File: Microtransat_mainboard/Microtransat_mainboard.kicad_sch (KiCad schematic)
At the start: 16 parts, among them J10 Conn_01x04, J2 Conn_01x02, J4 Conn_01x04, J5 Conn_01x05, J7 Conn_01x05, J9 Conn_01x04, SW1 SW_SPST, U5 SD Card Module

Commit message: add estop stuff kinda
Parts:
- removed J7: Conn_01x05, symbol Connector_Generic:Conn_01x05
- added J1: Conn_01x08, symbol Connector_Generic:Conn_01x08
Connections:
- net +5V: now also J1.1 (Pin_1)
- net GND: now also J1.2 (Pin_2)
- net INPWM0: now also J1.3 (Pin_3)
- net INPWM1: now also J1.4 (Pin_4)
- net MODE: now also J1.5 (Pin_5)
- net GPIO20: now reaches A1.26 (GPIO20)
- net GPIO21: now reaches A1.27 (GPIO21)
- new net eSTOPIN: J1.6 (Pin_6)
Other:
- sheet LED Interface renamed Relay Board Interface
- added sheet eStop Reading (estop_reading.kicad_sch)
- added sheet eStop Trigger (estop_trigger.kicad_sch)
- note removed: "Add all of the pins (6 total)"
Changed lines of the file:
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@@
 		)
 	)
-	(text "Add all of the pins (6 total)"
-		(exclude_from_sim no)
-		(at 82.55 128.016 0)
-		(effects
-			(font
-				(size 1.27 1.27)
-			)
-		)
-	)
 	(text "uses spi\nCS0\n"
 		(exclude_from_sim no)
@@
 		)
 	)
+	(label "GPIO20"
+		(at 144.78 45.72 0)
+		(effects
+			(font
+				(size 1.27 1.27)
+			)
+			(justify left bottom)
+		)
+	)
 	(label "PPS"
 		(at 172.72 114.3 180)
@@
 		)
 	)
+	(label "GPIO21"
+		(at 151.13 60.96 0)
+		(effects
+			(font
+				(size 1.27 1.27)
+			)
+			(justify left bottom)
+		)
+	)
 	(label "SCL"
 		(at 111.76 147.32 180)
@@
 		)
 	)
+	(label "GPIO20"
+		(at 218.44 119.38 0)
+		(effects
+			(font
+				(size 1.27 1.27)
+			)
+			(justify left bottom)
+		)
+	)
 	(label "CS1"
 		(at 51.435 186.69 0)
@@
 		)
 	)
+	(label "eSTOPIN"
+		(at 72.39 139.7 180)
+		(effects
+			(font
+				(size 1.27 1.27)
+			)
+			(justify right bottom)
+		)
+	)
 	(label "VREF"
 		(at 218.44 134.62 0)
@@
 		)
 	)
+	(label "GPIO21"
+		(at 218.44 121.92 0)
+		(effects
+			(font
+				(size 1.27 1.27)
+			)
+			(justify left bottom)
+		)
+	)
 	(label "MODE"
 		(at 172.72 127 180)
@@
 		)
 	)
+	(label "eSTOPIN"
+		(at 118.11 45.72 180)
+		(effects
+			(font
+				(size 1.27 1.27)
+			)
+			(justify right bottom)
+		)
+	)
 	(label "SDA"
 		(at 172.72 121.92 180)
@@
 	)
 	(symbol
-		(lib_id "Connector_Generic:Conn_01x05")
-		(at 77.47 132.08 0)
-		(unit 1)
-		(exclude_from_sim no)
-		(in_bom yes)
-		(on_board yes)
-		(dnp no)
-		(fields_autoplaced yes)
-		(property "Reference" "J7"
-			(at 80.01 130.8099 0)
-			(effects
-				(font
-					(size 1.27 1.27)
-				)
-				(justify left)
-			)
-		)
-		(property "Value" "Conn_01x05"
-			(at 80.01 133.3499 0)
-			(effects
-				(font
-					(size 1.27 1.27)
-				)
-				(justify left)
-			)
-		)
-		(property "Footprint" ""
-			(at 77.47 132.08 0)
-			(effects
-				(font
-					(size 1.27 1.27)
-				)
-				(hide yes)
-			)
-		)
-		(property "Datasheet" "~"
-			(at 77.47 132.08 0)
-			(effects
-				(font
-					(size 1.27 1.27)
-				)
-				(hide yes)
-			)
-		)
-		(property "Description" "Generic connector, single row, 01x05, script generated (kicad-library-utils/schlib/autogen/connector/)"
-			(at 77.47 132.08 0)
-			(effects
-				(font
-					(size 1.27 1.27)
-				)
-				(hide yes)
-			)
-		)
-		(pin "2"
-		)
-		(pin "1"
-		)
-		(pin "5"
-		)
-		(pin "3"
-		)
-		(pin "4"
-		)
-		(instances
-			(project ""
-				(path "/89914625-be83-416e-bb0d-b792f59b4aa6"
-					(reference "J7")
-					(unit 1)
-				)
-			)
-		)
-	)
-	(symbol
 		(lib_id "power:+5V")
 		(at 190.5 83.82 0)
@@
 	)
 	(symbol
+		(lib_id "Connector_Generic:Conn_01x08")
+		(at 77.47 134.62 0)
+		(unit 1)
+		(exclude_from_sim no)
+		(in_bom yes)
+		(on_board yes)
+		(dnp no)
+		(fields_autoplaced yes)
+		(property "Reference" "J1"
+			(at 80.01 134.6199 0)
+			(effects
+				(font
+					(size 1.27 1.27)
+				)
+				(justify left)
+			)
+		)
+		(property "Value" "Conn_01x08"
+			(at 80.01 137.1599 0)
+			(effects
+				(font
+					(size 1.27 1.27)
+				)
+				(justify left)
+			)
+		)
+		(property "Footprint" ""
+			(at 77.47 134.62 0)
+			(effects
+				(font
+					(size 1.27 1.27)
+				)
+				(hide yes)
+			)
+		)
+		(property "Datasheet" "~"
+			(at 77.47 134.62 0)
+			(effects
+				(font
+					(size 1.27 1.27)
+				)
+				(hide yes)
+			)
+		)
+		(property "Description" "Generic connector, single row, 01x08, script generated (kicad-library-utils/schlib/autogen/connector/)"
+			(at 77.47 134.62 0)
+			(effects
+				(font
+					(size 1.27 1.27)
+				)
+				(hide yes)
+			)
+		)
+		(pin "5"
+		)
+		(pin "1"
+		)
+		(pin "2"
+		)
+		(pin "3"
+		)
+		(pin "4"
+		)
+		(pin "6"
+		)
+		(pin "7"
+		)
+		(pin "8"
+		)
+		(instances
+			(project ""
+				(path "/89914625-be83-416e-bb0d-b792f59b4aa6"
+					(reference "J1")
+					(unit 1)
+				)
+			)
+		)
+	)
+	(symbol
 		(lib_id "Device:R")
 		(at 24.13 82.55 0)
@@
 			(color 0 0 0 0.0000)
 		)
-		(property "Sheetname" "LED Interface"
+		(property "Sheetname" "Relay Board Interface"
 			(at 241.3 107.2384 0)
 			(effects
@@
 	)
 	(sheet
+		(at 118.11 58.42)
+		(size 33.02 5.08)
+		(exclude_from_sim no)
+		(in_bom yes)
+		(on_board yes)
+		(dnp no)
+		(fields_autoplaced yes)
+		(stroke
+			(width 0.1524)
+			(type solid)
+		)
+		(fill
+			(color 0 0 0 0.0000)
+		)
+		(property "Sheetname" "eStop Reading"
+			(at 118.11 57.7084 0)
+			(effects
+				(font
+					(size 1.27 1.27)
+				)
+				(justify left bottom)
+			)
+		)
+		(property "Sheetfile" "estop_reading.kicad_sch"
+			(at 118.11 64.0846 0)
+			(effects
+				(font
+					(size 1.27 1.27)
+				)
+				(justify left top)
+			)
+		)
+		(pin "estop_signal" output
+			(at 151.13 60.96 0)
+			(effects
+				(font
+					(size 1.27 1.27)
+				)
+				(justify right)
+			)
+		)
+		(instances
+			(project "Microtransat_mainboard"
+				(path "/89914625-be83-416e-bb0d-b792f59b4aa6"
+					(page "4")
+				)
+			)
+		)
+	)
+	(sheet
 		(at 121.92 105.41)
 		(size 25.4 10.16)
@@
 				)
 			)
+		)
+	)
+	(sheet
+		(at 118.11 43.18)
+		(size 26.67 5.08)
+		(exclude_from_sim no)
+		(in_bom yes)
+		(on_board yes)
+		(dnp no)
+		(fields_autoplaced yes)
+		(stroke
+			(width 0.1524)
+			(type solid)
+		)
+		(fill
+			(color 0 0 0 0.0000)
+		)
+		(property "Sheetname" "eStop Trigger"
+			(at 118.11 42.4684 0)
+			(effects
+				(font
+					(size 1.27 1.27)
+				)
+				(justify left bottom)
+			)
+		)
+		(property "Sheetfile" "estop_trigger.kicad_sch"
+			(at 118.11 48.8446 0)
+			(effects
+				(font
+					(size 1.27 1.27)
+				)
+				(justify left top)
+			)
+		)
+		(pin "OUT" output
+			(at 144.78 45.72 0)
+			(effects
+				(font
+					(size 1.27 1.27)
+				)
+				(justify right)
+			)
+		)
+		(pin "RC_IN" input
+			(at 118.11 45.72 180)
+			(effects
+				(font
+					(size 1.27 1.27)
+				)
+				(justify left)
+			)
+		)
+		(instances
+			(project "Microtransat_mainboard"
+				(path "/89914625-be83-416e-bb0d-b792f59b4aa6"
+					(page "5")
+				)
+			)

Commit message: puh
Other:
- sheet Relay Board Interface ports: added eStopTrigger; removed none
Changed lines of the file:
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@@
 	(wire
 		(pts
+			(xy 262.89 110.49) (xy 266.7 110.49)
+		)
+		(stroke
+			(width 0)
+			(type default)
+		)
+	)
+	(wire
+		(pts
 			(xy 24.13 86.36) (xy 24.13 87.63)
 		)
@@
 	(wire
 		(pts
+			(xy 266.7 45.72) (xy 144.78 45.72)
+		)
+		(stroke
+			(width 0)
+			(type default)
+		)
+	)
+	(wire
+		(pts
+			(xy 266.7 110.49) (xy 266.7 45.72)
+		)
+		(stroke
+			(width 0)
+			(type default)
+		)
+	)
+	(wire
+		(pts
 			(xy 24.13 97.79) (xy 24.13 100.33)
 		)
@@
 			)
 		)
+		(pin "eStopTrigger" input
+			(at 262.89 110.49 0)
+			(effects
+				(font
+					(size 1.27 1.27)
+				)
+				(justify right)
+			)
+		)

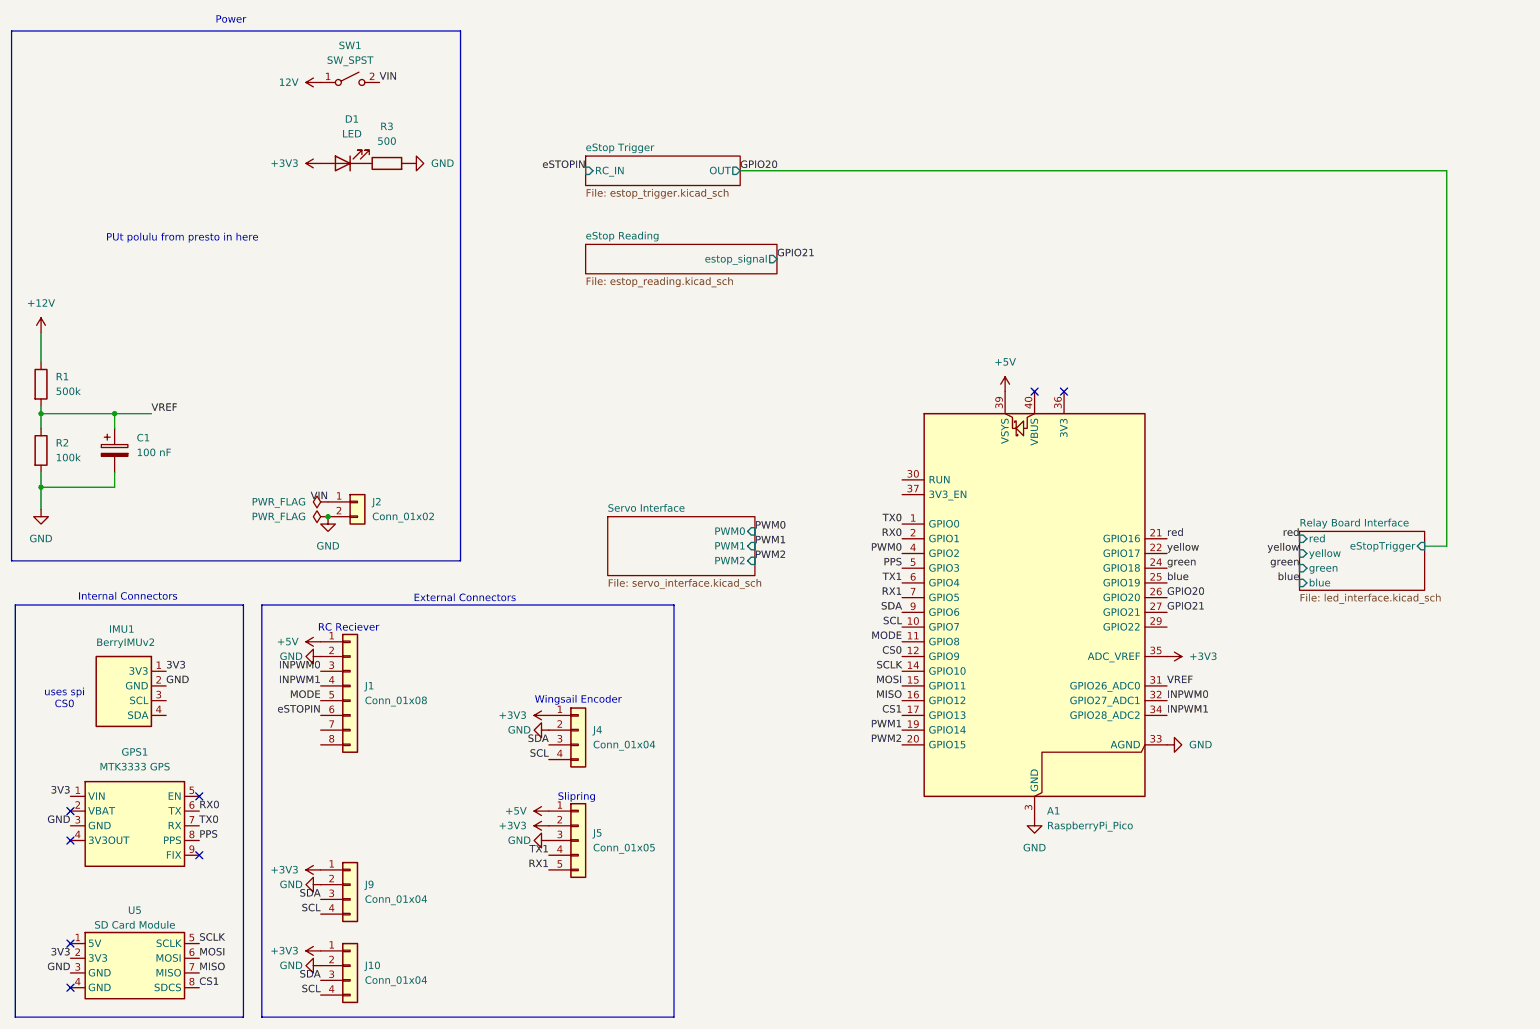
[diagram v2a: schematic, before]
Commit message: Added new IMU to the schematic + new PWM
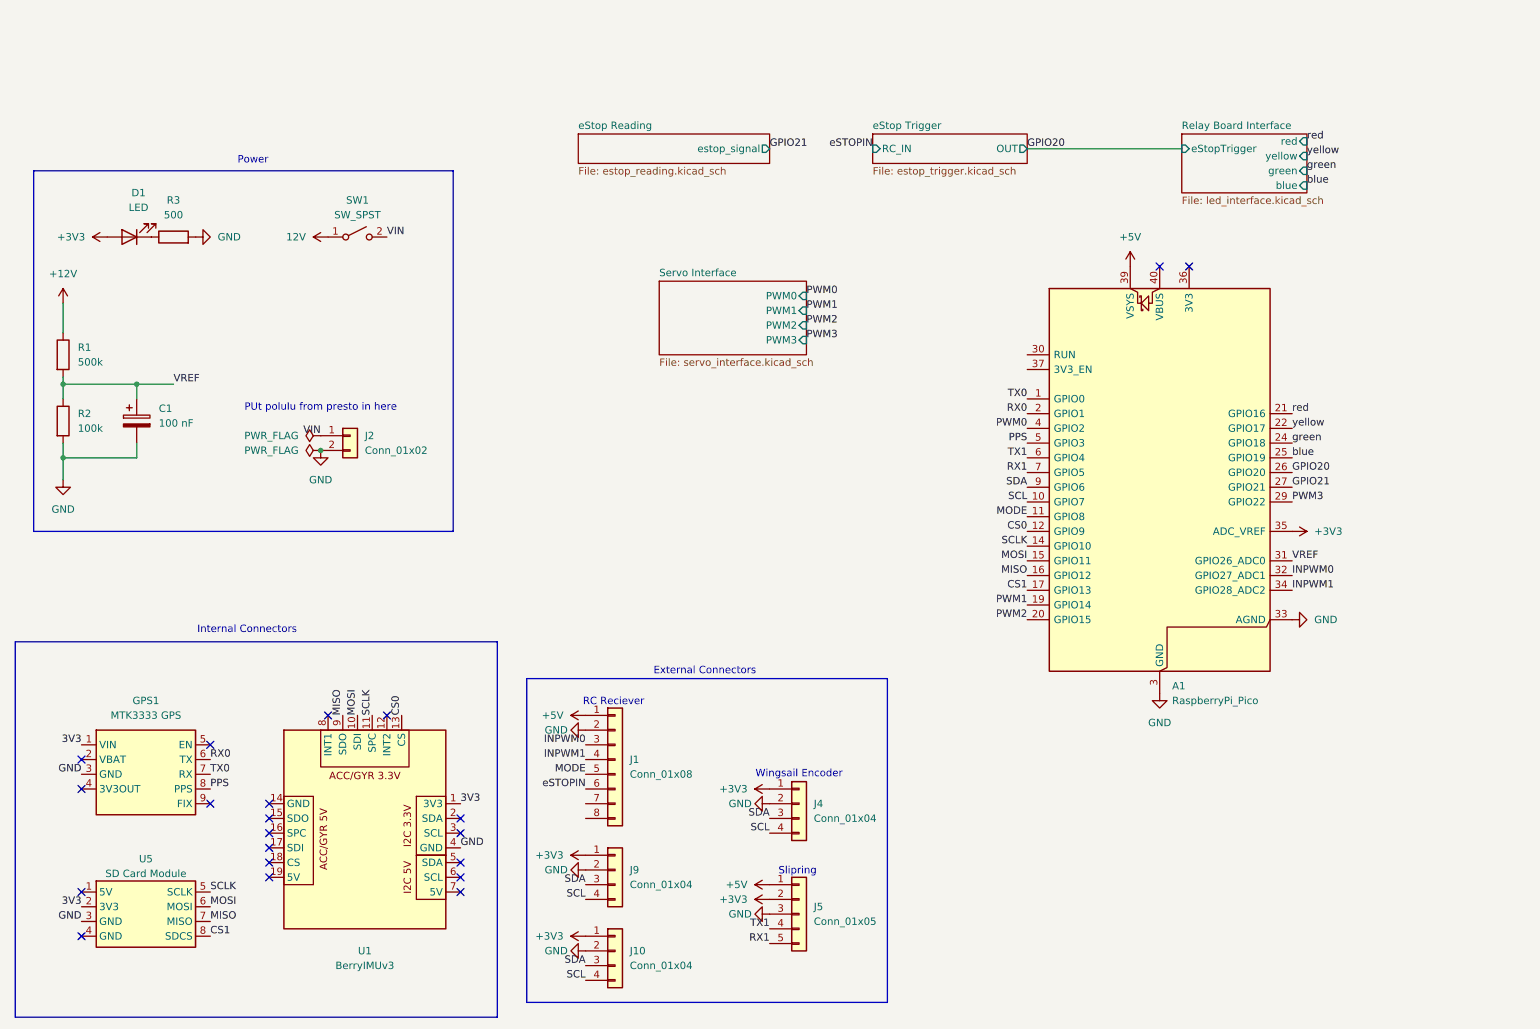
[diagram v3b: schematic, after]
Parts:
- removed IMU1: BerryIMUv2, symbol Microtransat:BerryIMUv2
- added U1: BerryIMUv3, Microtransat:BerryIMUv3, symbol Microtransat:BerryIMUv3
- GPS1: footprint (none) -> Microtransat:MTK3333
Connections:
- net 3V3: now also U1.1 (3V3)
- net CS0: now also U1.13 (CS)
- net GND: now also U1.4 (GND)
- net MISO: now also U1.9 (SDO)
- net MOSI: now also U1.10 (SDI)
- net SCLK: now also U1.11 (SPC)
- net PWM3: now reaches A1.29 (GPIO22)
- no-connect marks 8 -> 21
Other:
- sheet Servo Interface ports: added PWM3; removed none
- note removed: "uses spi CS0"
- moved on the sheet: A1, C1, D1, GPS1, J1, J10, J2, J4, J5, J9, R1, R2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

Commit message: Added regulators and updated GPS, IMU, SD Card symbols
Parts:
- removed GPS1: MTK3333 GPS, Microtransat:MTK3333, symbol Microtransat:MTK3333_GPS
- removed U1: BerryIMUv3, Microtransat:BerryIMUv3, symbol Microtransat:BerryIMUv3
- removed U5: SD Card Module, Adafruit 254:Adafruit_254, symbol Microtransat:SD Card Module
- added D101: 1N5817, Diode_THT:D_DO-41_SOD81_P10.16mm_Horizontal, symbol Diode:1N5817
- added J101: 12V IN, Connector_AMASS:AMASS_XT30PW-M_1x02_P2.50mm_Horizontal, symbol Connector:Conn_01x02_Pin
- added U1: GPS 746, Microtransat:XCVR_746, symbol 746:746
- added U2: SD Card Module 254, Microtransat:MODULE_254, symbol 254:254
- added U3: IMU 4754, Microtransat:MODULE_4754, symbol 4754:4754
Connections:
- net +12V: now also D101.1 (K)
- net 3V3: now also U1.8 (VIN), U2.7 (3V), U3.JP1_1 (VIN), U3.JP2_2 (P0), U3.JP2_3 (P1), U3.JP2_4 (~{RST})
- net CS0: now also U3.JP2_6 (CS)
- net CS1: now also U2.2 (CS)
- net GND: now also J101.1 (Pin_1), U1.7 (GND), U1.SH1 (SHIELD), U1.SH2 (SHIELD), U2.6 (GND), U3.JP1_3 (GND)
- net MISO: now also U2.4 (DO), U3.JP1_5 (SDA)
- net MOSI: now also U2.3 (DI), U3.JP2_5 (DI)
- net PPS: now also U1.9 (PPS)
- net RX0: now also U1.5 (TX)
- net SCLK: now also U2.5 (CLK), U3.JP1_4 (SCL)
- net TX0: now also U1.6 (RX)
- new net: D101.2 (A), J101.2 (Pin_2)
- no-connect marks 21 -> 11
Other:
- added sheet Regulators (regulators.kicad_sch)
